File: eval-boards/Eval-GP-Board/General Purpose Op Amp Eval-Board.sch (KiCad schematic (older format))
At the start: 3 parts, among them J1 IN, J2 Conn_01x03_Male, J3 OUT

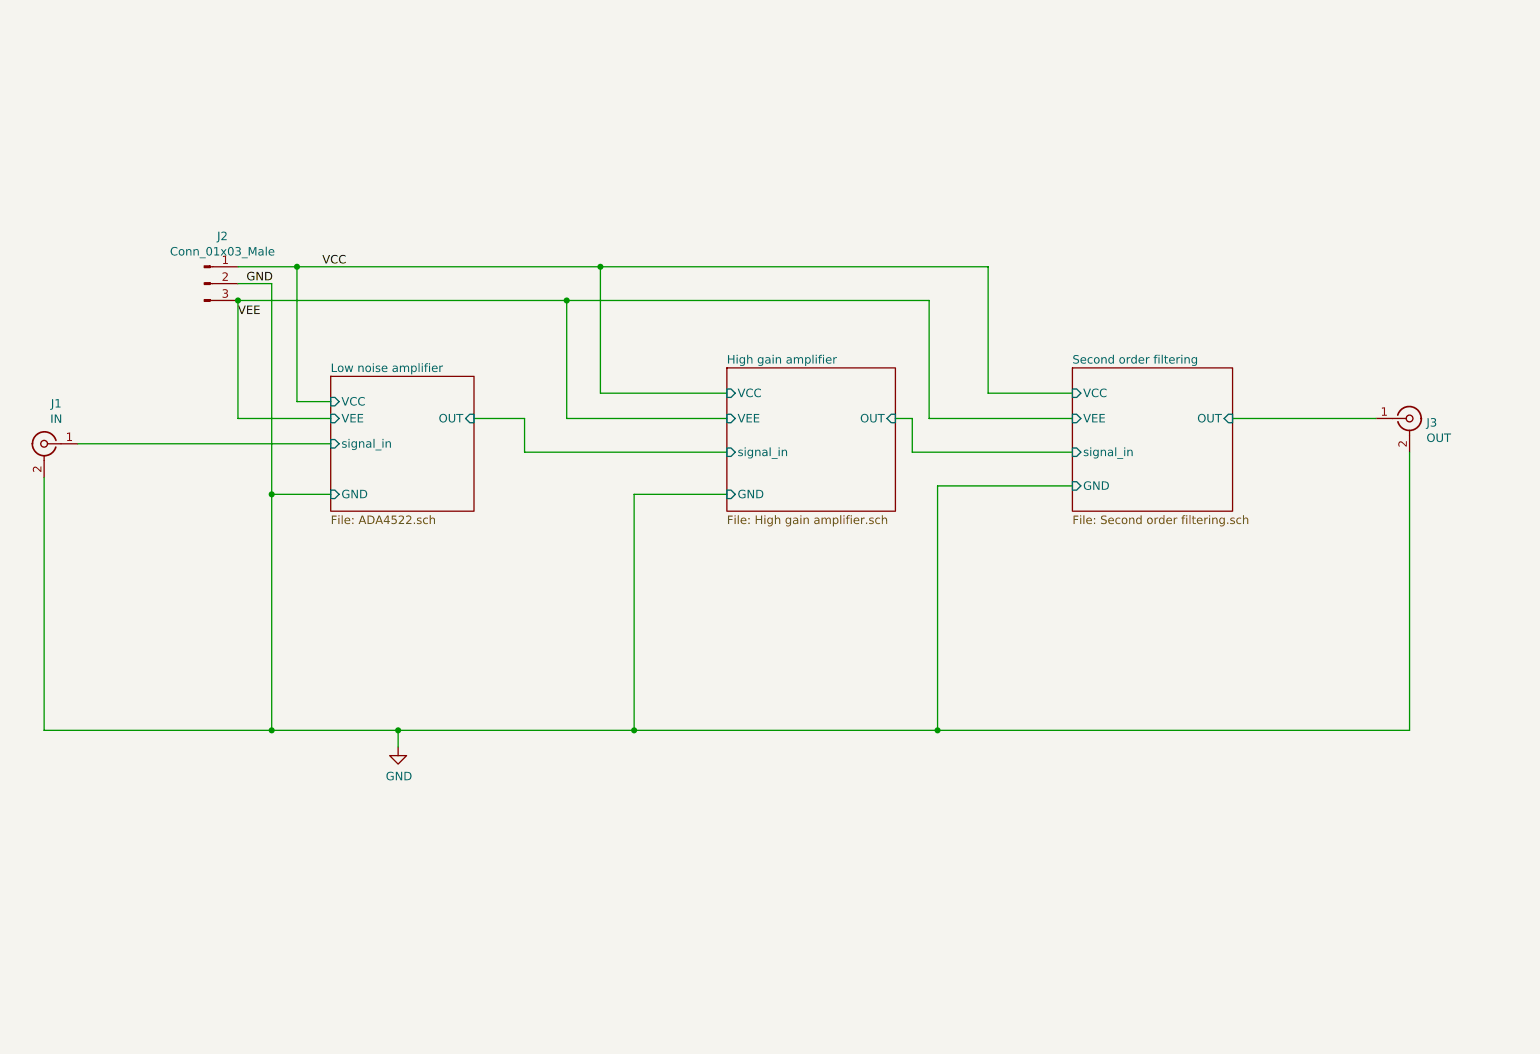
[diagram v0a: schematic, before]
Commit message: Updated schematic
均采用双运放，前级4522可以单运放工作也可以级联工作
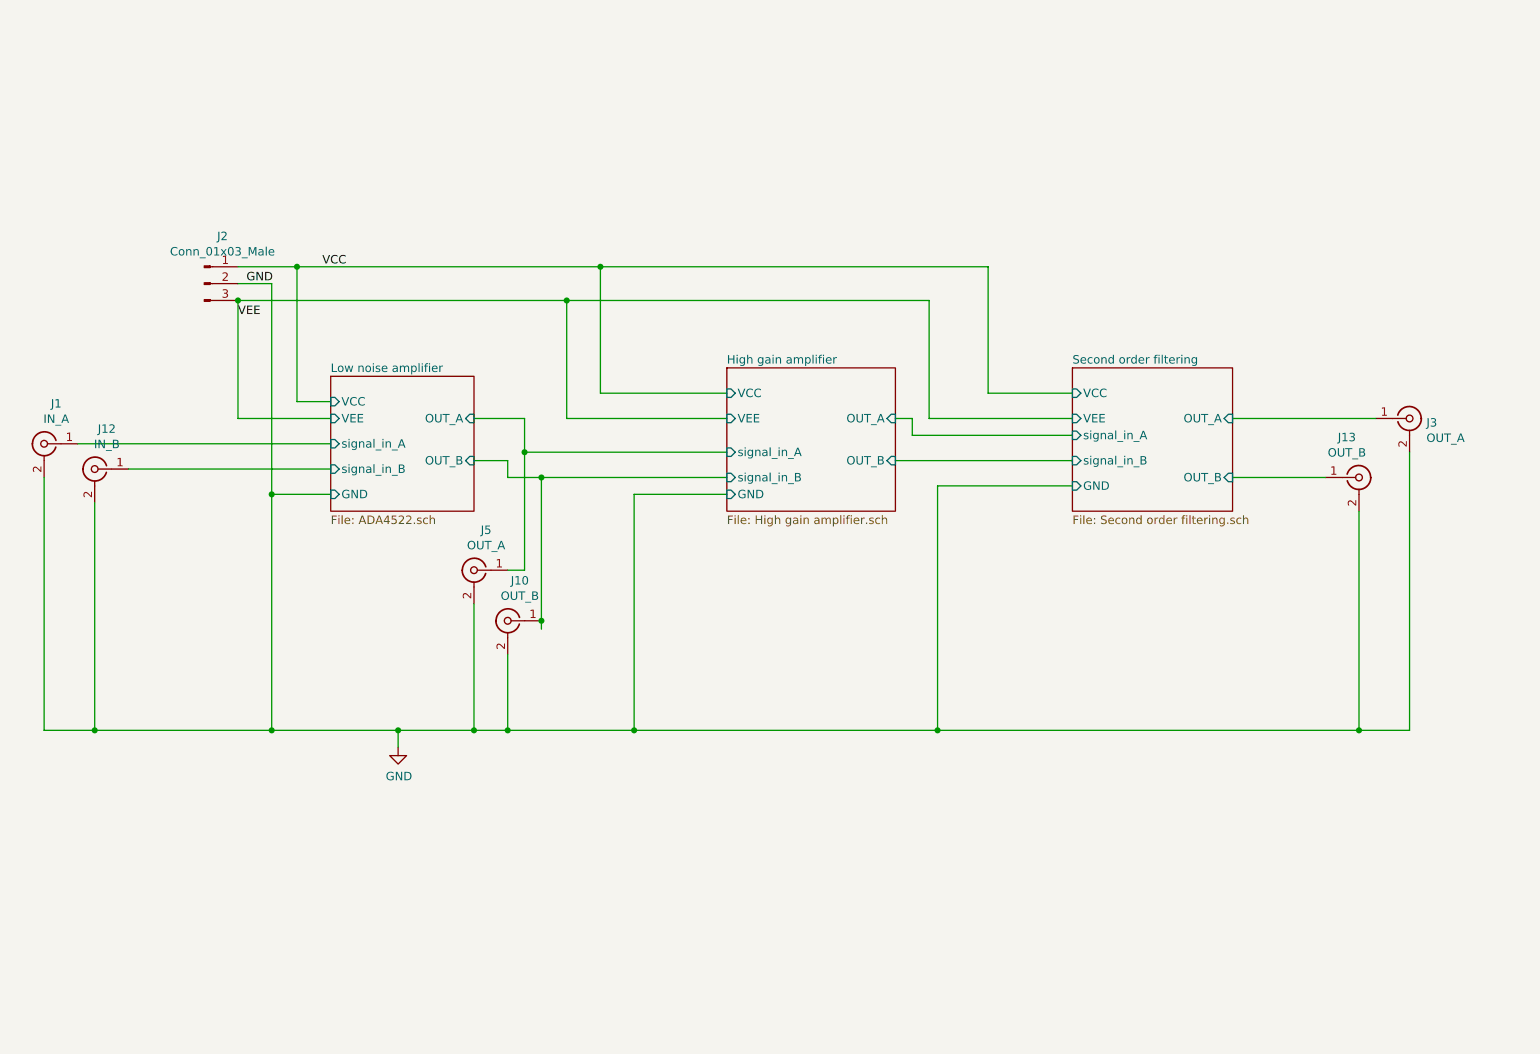
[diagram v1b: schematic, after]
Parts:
- added J10, J13: OUT_B, Connector_Coaxial:SMA_Amphenol_901-144_Vertical, symbol Connector:Conn_Coaxial
- added J12: IN_B, Connector_Coaxial:SMA_Amphenol_901-144_Vertical, symbol Connector:Conn_Coaxial
- added J5: OUT_A, Connector_Coaxial:SMA_Amphenol_901-144_Vertical, symbol Connector:Conn_Coaxial
- J1: value IN -> IN_A
- J3: value OUT -> OUT_A
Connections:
- net GND: now also J10.2 (Ext), J12.2 (Ext), J13.2 (Ext), J5.2 (Ext)
- net Low noise amplifier/signal_in renamed Low noise amplifier/signal_in_A
- net Second order filtering/OUT renamed Second order filtering/OUT_A
- new net High gain amplifier/signal_in_A: J5.1 (In)
- new net High gain amplifier/signal_in_B: J10.1 (In)
- new net Low noise amplifier/signal_in_B: J12.1 (In)
- new net Second order filtering/OUT_B: J13.1 (In)
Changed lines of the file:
@@
 EESchema Schematic File Version 4
+LIBS:General Purpose Op Amp Eval-Board-cache
 EELAYER 29 0
 EELAYER END
@@
 F2 "VCC" I L 7700 2950 50
 F3 "VEE" I L 7700 3100 50
-F4 "signal_in" I L 7700 3300 50
+F4 "signal_in_A" I L 7700 3200 50
 F5 "GND" I L 7700 3500 50
-F6 "OUT" I R 8650 3100 50
+F6 "OUT_A" I R 8650 3100 50
+F7 "signal_in_B" I L 7700 3350 50
+F8 "OUT_B" I R 8650 3450 50
 $EndSheet
 Wire Wire Line
@@
 Connection ~ 4700 2400
 Wire Wire Line
-	7700 3300 6750 3300
-Wire Wire Line
-	6750 3300 6750 3100
-Wire Wire Line
 	6750 3100 6650 3100
 Wire Wire Line
@@
 Connection ~ 2950 4950
 Wire Wire Line
-	1600 4950 2950 4950
+	1600 4950 1900 4950
 Wire Wire Line
 	6900 3500 6900 4950
@@
 Connection ~ 5100 4950
 Connection ~ 3700 4950
-Wire Wire Line
-	3700 4950 5100 4950
 Wire Wire Line
 	5100 3550 5100 4950
@@
 F2 "VCC" I L 3300 3000 50
 F3 "VEE" I L 3300 3100 50
-F4 "signal_in" I L 3300 3250 50
+F4 "signal_in_A" I L 3300 3250 50
 F5 "GND" I L 3300 3550 50
-F6 "OUT" I R 4150 3100 50
+F6 "OUT_A" I R 4150 3100 50
+F7 "signal_in_B" I L 3300 3400 50
+F8 "OUT_B" I R 4150 3350 50
 $EndSheet
 $Sheet
@@
 F2 "VCC" I L 5650 2950 50
 F3 "VEE" I L 5650 3100 50
-F4 "signal_in" I L 5650 3300 50
+F4 "signal_in_A" I L 5650 3300 50
 F5 "GND" I L 5650 3550 50
-F6 "OUT" I R 6650 3100 50
+F6 "OUT_A" I R 6650 3100 50
+F7 "signal_in_B" I L 5650 3450 50
+F8 "OUT_B" I R 6650 3350 50
 $EndSheet
 Text Label 3250 2200 0    50   ~ 0
@@
 	9700 3300 9700 4950
 Wire Wire Line
-	9700 4950 6900 4950
+	9700 4950 9400 4950
 Connection ~ 6900 4950
 Wire Wire Line
@@
 P 9700 3100
 F 0 "J3" H 9800 3075 50  0000 L CNN
-F 1 "OUT" H 9800 2984 50  0000 L CNN
+F 1 "OUT_A" H 9800 2984 50  0000 L CNN
 F 2 "Connector_Coaxial:SMA_Amphenol_901-144_Vertical" H 9700 3100 50  0001 C CNN
 F 3 " ~" H 9700 3100 50  0001 C CNN
@@
 P 1600 3250
 F 0 "J1" H 1528 3488 50  0000 C CNN
-F 1 "IN" H 1528 3397 50  0000 C CNN
+F 1 "IN_A" H 1528 3397 50  0000 C CNN
 F 2 "Connector_Coaxial:SMA_Amphenol_901-144_Vertical" H 1600 3250 50  0001 C CNN
 F 3 " ~" H 1600 3250 50  0001 C CNN
@@
 	-1   0    0    -1
 $EndComp
+$Comp
+L Connector:Conn_Coaxial J12
+U 1 1 5D1EC923
+P 1900 3400
+F 0 "J12" H 1828 3638 50  0000 C CNN
+F 1 "IN_B" H 1828 3547 50  0000 C CNN
+F 2 "Connector_Coaxial:SMA_Amphenol_901-144_Vertical" H 1900 3400 50  0001 C CNN
+F 3 " ~" H 1900 3400 50  0001 C CNN
+	1    1900 3400
+	-1   0    0    -1
+$EndComp
+Wire Wire Line
+	1900 3600 1900 4950
+Connection ~ 1900 4950
+Wire Wire Line
+	1900 4950 2950 4950
+Wire Wire Line
+	2100 3400 3300 3400
+$Comp
+L Connector:Conn_Coaxial J13
+U 1 1 5D1EE33D
+P 9400 3450
+F 0 "J13" H 9328 3688 50  0000 C CNN
+F 1 "OUT_B" H 9328 3597 50  0000 C CNN
+F 2 "Connector_Coaxial:SMA_Amphenol_901-144_Vertical" H 9400 3450 50  0001 C CNN
+F 3 " ~" H 9400 3450 50  0001 C CNN
+	1    9400 3450
+	1    0    0    -1
+$EndComp
+Wire Wire Line
+	9400 3650 9400 4950
+Connection ~ 9400 4950
+Wire Wire Line
+	9400 4950 6900 4950
+Wire Wire Line
+	4150 3350 4350 3350
+Wire Wire Line
+	4350 3350 4350 3450
+$Comp
+L Connector:Conn_Coaxial J5
+U 1 1 5D23A4DA
+P 4150 4000
+F 0 "J5" H 4078 4238 50  0000 C CNN
+F 1 "OUT_A" H 4078 4147 50  0000 C CNN
+F 2 "Connector_Coaxial:SMA_Amphenol_901-144_Vertical" H 4150 4000 50  0001 C CNN
+F 3 " ~" H 4150 4000 50  0001 C CNN
+	1    4150 4000
+	-1   0    0    -1
+$EndComp
+$Comp
+L Connector:Conn_Coaxial J10
+U 1 1 5D23BCD4
+P 4350 4300
+F 0 "J10" H 4278 4538 50  0000 C CNN
+F 1 "OUT_B" H 4278 4447 50  0000 C CNN
+F 2 "Connector_Coaxial:SMA_Amphenol_901-144_Vertical" H 4350 4300 50  0001 C CNN
+F 3 " ~" H 4350 4300 50  0001 C CNN
+	1    4350 4300
+	-1   0    0    -1
+$EndComp
+Wire Wire Line
+	3700 4950 4150 4950
+Connection ~ 4150 4950
+Wire Wire Line
+	4150 4950 4350 4950
+Wire Wire Line
+	4350 4500 4350 4950
+Connection ~ 4350 4950
+Wire Wire Line
+	4350 4950 5100 4950
+Wire Wire Line
+	4150 4200 4150 4950
+Wire Wire Line
+	4350 4000 4450 4000
+Wire Wire Line
+	4450 4000 4450 3300
+Connection ~ 4450 3300
+Wire Wire Line
+	4550 4350 4550 4300
+Wire Wire Line
+	4350 3450 4550 3450
+Connection ~ 4550 3450
+Wire Wire Line
+	4550 3450 5650 3450
+Connection ~ 4550 4300
+Wire Wire Line
+	4550 4300 4550 3450
+Wire Wire Line
+	6750 3100 6750 3200
+Wire Wire Line
+	6750 3200 7700 3200
+Wire Wire Line
+	6650 3350 7700 3350
+Wire Wire Line
+	8650 3450 9200 3450
 $EndSCHEMATC

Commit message: 双通道通用精密放大器PCB
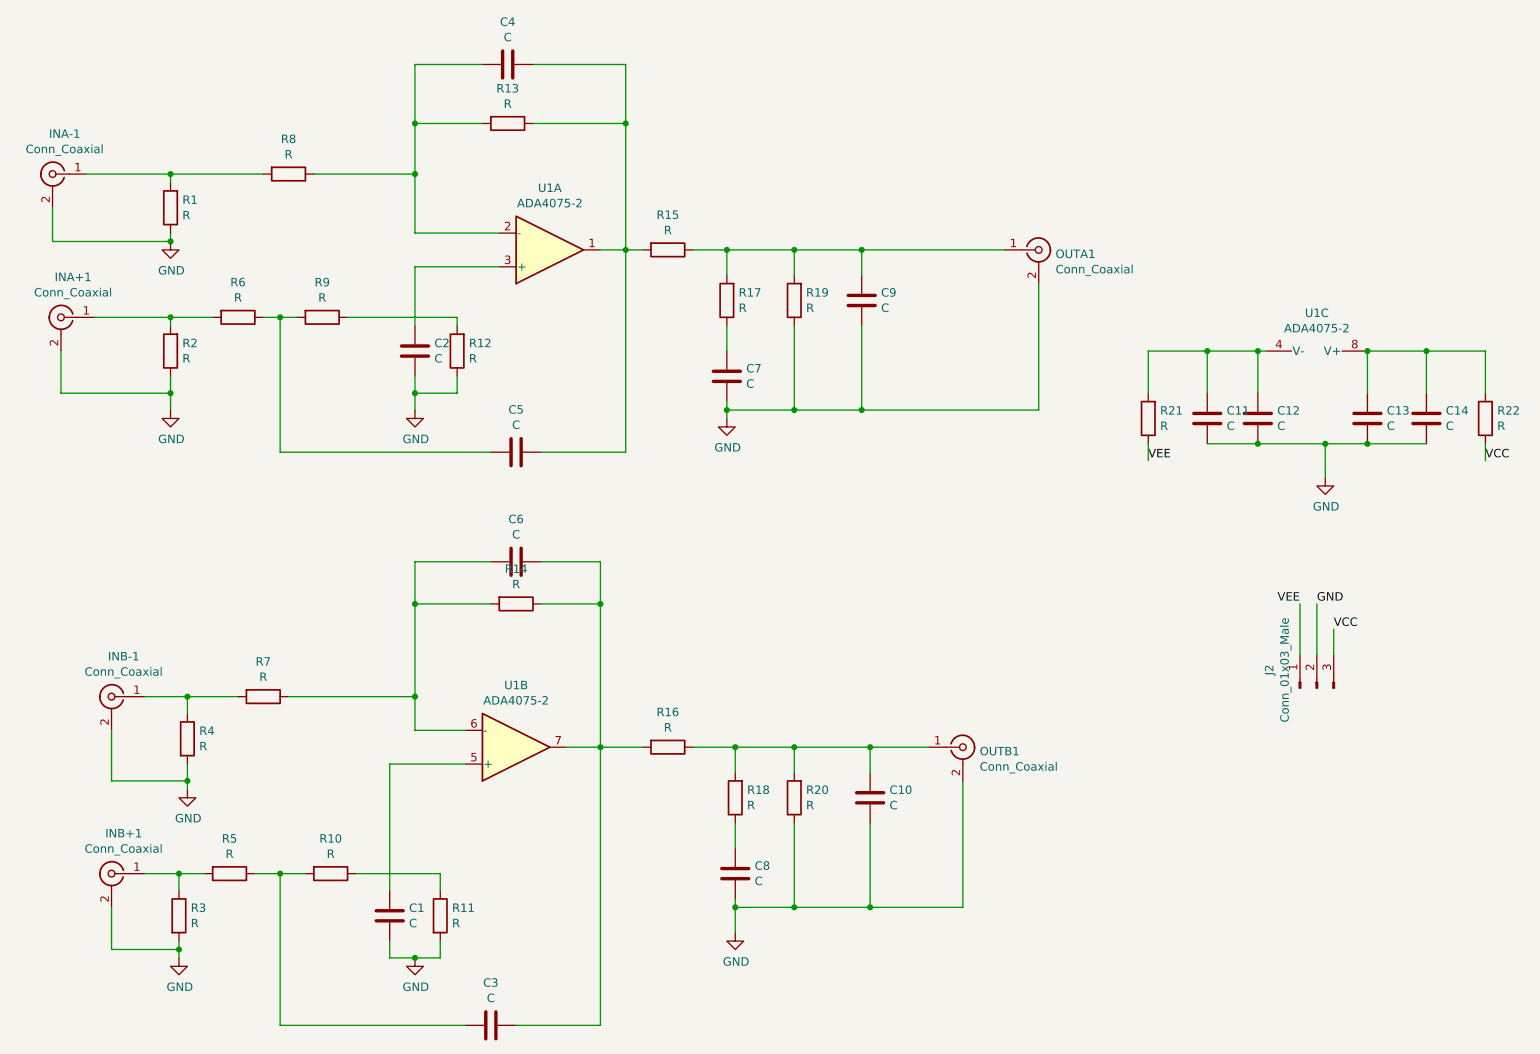
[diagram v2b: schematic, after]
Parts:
- removed J1: IN_A, Connector_Coaxial:SMA_Amphenol_901-144_Vertical, symbol Connector:Conn_Coaxial
- removed J10, J13: OUT_B, Connector_Coaxial:SMA_Amphenol_901-144_Vertical, symbol Connector:Conn_Coaxial
- removed J12: IN_B, Connector_Coaxial:SMA_Amphenol_901-144_Vertical, symbol Connector:Conn_Coaxial
- removed J3, J5: OUT_A, Connector_Coaxial:SMA_Amphenol_901-144_Vertical, symbol Connector:Conn_Coaxial
- added C1, C10, C11, C12, C13, C14, C2, C3, C4, C5, C6, C7, C8, C9: C, Capacitor_SMD:C_0603_1608Metric_Pad1.05x0.95mm_HandSolder, symbol Device:C
- added INA+1, INA-1, INB+1, INB-1, OUTA1, OUTB1: Conn_Coaxial, Connector_Coaxial:SMA_Amphenol_132134-11_Vertical, symbol Connector:Conn_Coaxial
- added R1, R10, R11, R12, R13, R14, R15, R16, R17, R18, R19, R2, R20, R21, R22, R3, R4, R5, R6, R7, R8, R9: R, Resistor_SMD:R_0603_1608Metric_Pad1.05x0.95mm_HandSolder, symbol Device:R
- added U1: ADA4075-2, Package_SO:SOIC-8_3.9x4.9mm_P1.27mm, symbol Amplifier_Operational:ADA4075-2
- J2: footprint Connector_PinSocket_2.54mm:PinSocket_1x03_P2.54mm_Vertical -> Connector_JST:JST_XH_B3B-XH-A_1x03_P2.50mm_Vertical
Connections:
- net GND: now also C1.1, C10.1, C11.1, C12.1, C13.1, C14.1, C2.2, C7.1, C8.1, C9.1, INA+1.2 (Ext), INA-1.2 (Ext), INB+1.2 (Ext), INB-1.2 (Ext), OUTA1.2 (Ext), OUTB1.2 (Ext), R1.1, R11.2, R12.1, R19.1, R2.1, R20.1, R3.2, R4.2
- net VCC: now also J2.3 (Pin_3), R22.1; no longer J2.1 (Pin_1)
- net VEE: now also J2.1 (Pin_1), R21.1; no longer J2.3 (Pin_3)
- new net: C4.1, C5.1, R13.1, R15.2, U1.1
- new net: C4.2, R13.2, R8.1, U1.2 (-)
- new net: C2.1, U1.3 (+)
- new net: C1.2, U1.5 (+)
- new net: C6.2, R14.2, R7.1, U1.6 (-)
- new net: C3.1, C6.1, R14.1, R16.2, U1.7
- new net: C11.2, C12.2, R21.2, U1.4 (V-)
- new net: C13.2, C14.2, R22.2, U1.8 (V+)
- new net: INA-1.1 (In), R1.2, R8.2
- new net: INA+1.1 (In), R2.2, R6.2
- new net: C9.2, OUTA1.1 (In), R15.1, R17.2, R19.2
- new net: C5.2, R6.1, R9.2
- new net: R12.2, R9.1
- new net: C7.2, R17.1
- new net: INB-1.1 (In), R4.1, R7.2
- new net: INB+1.1 (In), R3.1, R5.2
- new net: C3.2, R10.2, R5.1
- new net: R10.1, R11.1
- new net: C10.2, OUTB1.1 (In), R16.1, R18.2, R20.2
- new net: C8.2, R18.1
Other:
- moved on the sheet: J2
